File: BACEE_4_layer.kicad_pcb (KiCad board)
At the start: 2 copper layers, 40.6 x 26.7 mm, 17 parts, among them J1 Serial, J2 Digital pins, J3 ICSP, J4 I2C, U1 DS1337S+, U2 24LC1025, U3 24LC1025, U4 ATMEGA328P-AU, Y1 Crystal 32MHz, Y2 Crystal 16MHz

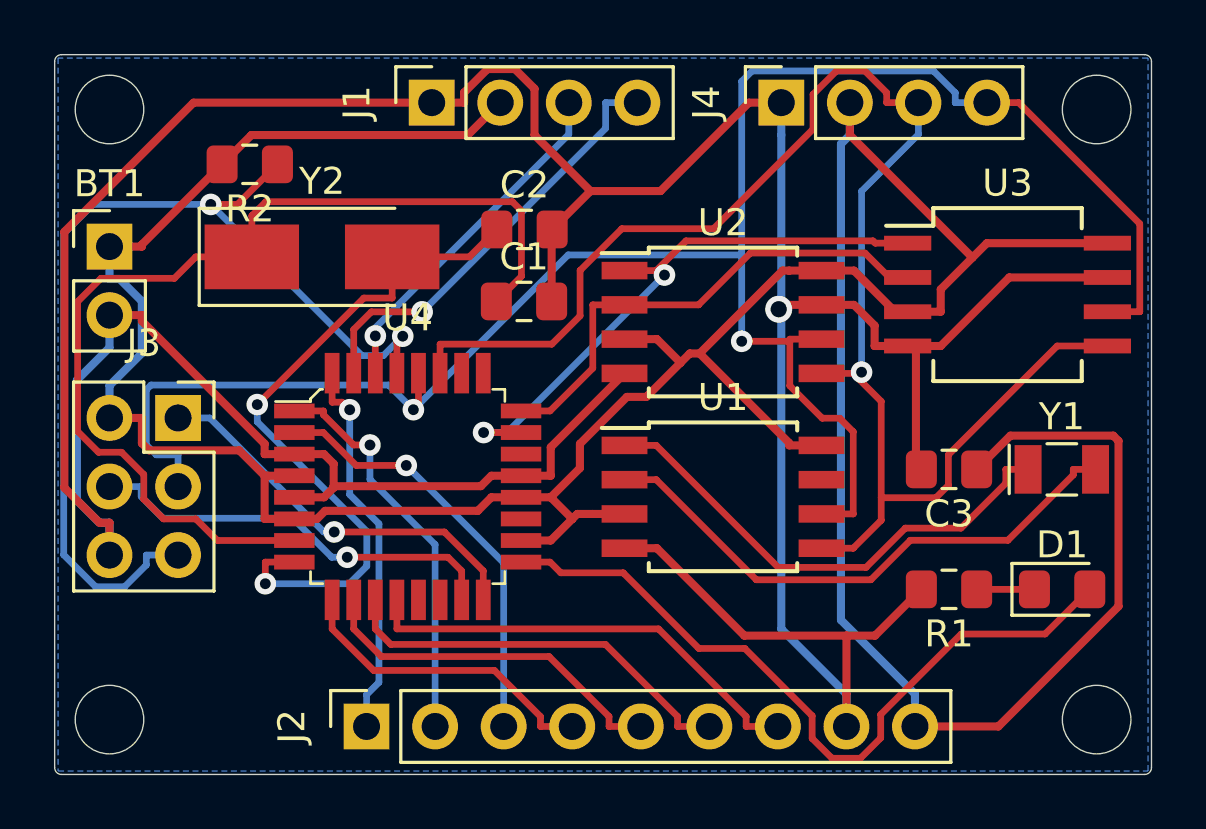
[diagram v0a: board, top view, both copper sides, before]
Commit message: Created copper field ares
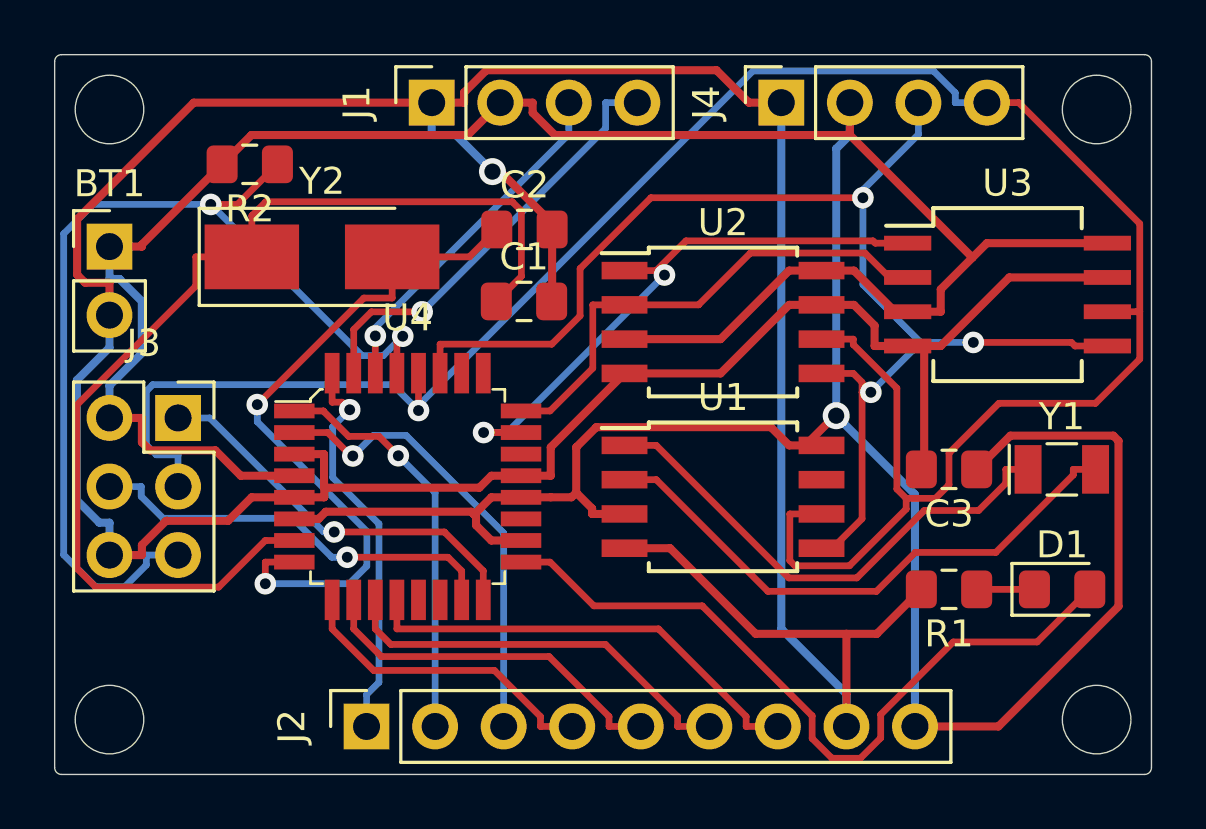
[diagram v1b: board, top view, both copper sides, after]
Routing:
- net /SCK: track 74.4 -> 85.2 mm, vias 2 -> 1
- net /Vcc: track 139.1 -> 149.3 mm, vias 0 -> 1
- net /SDA: track 57.7 -> 49.2 mm, vias 1 -> 3
- net Net-(C1-Pad1): track 37.8 -> 40.1 mm
- net GNDPWR: track 147.4 -> 145.2 mm
- net /D4: track 15.8 -> 17.1 mm
- net /D2: track 14.2 -> 14.7 mm
- removed copper zone on B.Cu, net GNDPWR
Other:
- copper layers 2 -> 4
